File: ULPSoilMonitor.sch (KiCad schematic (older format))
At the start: 21 parts, among them Q3 BC817, Q4 MMDT3904, SW1 RESET, U1 ESP32-WROOM-32, U2 MCP73123

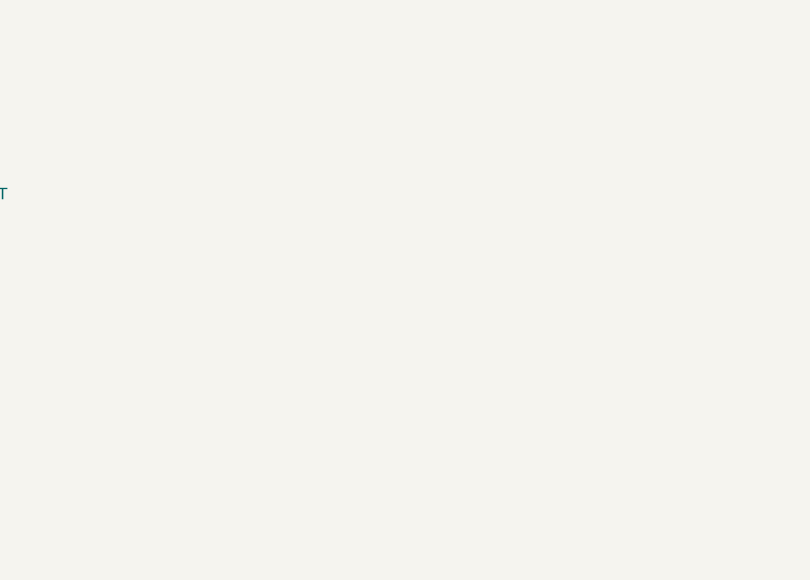
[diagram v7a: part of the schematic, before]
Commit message: Add USB-C connector
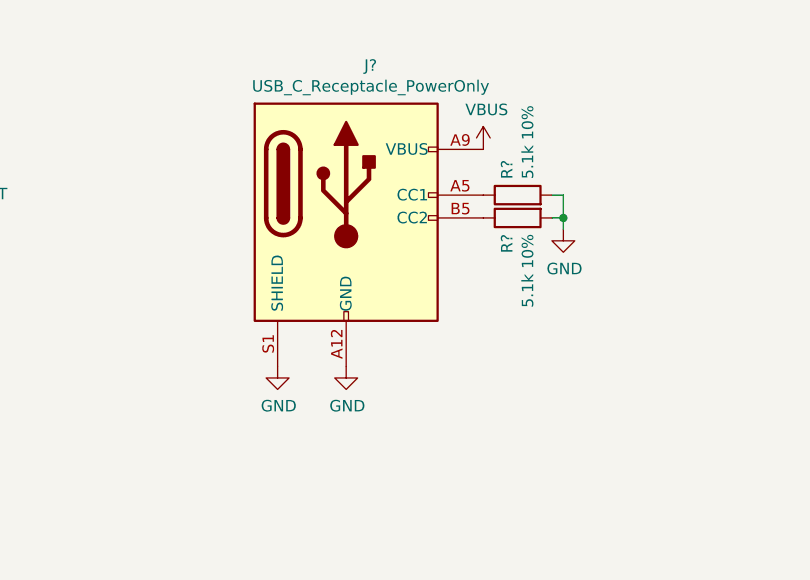
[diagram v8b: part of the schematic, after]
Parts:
- added J?: USB_C_Receptacle_PowerOnly, 0 - GIE Connectors, Terminal Blocks:TYPE-C-31-M-17.kicad_mod, symbol 0-GIE_Connector_Debug:USB_C_Receptacle_PowerOnly
- added R? (x2): 5.1k 10%, Resistor_SMD:R_0805_2012Metric, symbol Device:R
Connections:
- net -BATT: now also J?.A12 (GND), J?.B12 (GND), J?.S1 (SHIELD), R?.2, R?.2
- net VBUS: now also J?.A9 (VBUS), J?.B9 (VBUS)
- new net: J?.A5 (CC1), R?.1
- new net: J?.B5 (CC2), R?.1
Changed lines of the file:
@@
 Wire Wire Line
 	9400 5900 9400 6200
+$Comp
+L 0-GIE_Connector_Debug:USB_C_Receptacle_PowerOnly J?
+U 1 1 60612B67
+P 8500 1300
+F 0 "J?" H 8607 1817 50  0000 C CNN
+F 1 "USB_C_Receptacle_PowerOnly" H 8607 1726 50  0000 C CNN
+F 2 "0 - GIE Connectors, Terminal Blocks:TYPE-C-31-M-17.kicad_mod" H 8650 1800 50  0001 C CNN
+F 3 "https://www.usb.org/sites/default/files/documents/usb_type-c.zip" H 8650 1300 50  0001 C CNN
+	1    8500 1300
+	1    0    0    -1
+$EndComp
+$Comp
+L power:GND #PWR?
+U 1 1 60613D10
+P 8200 2100
+F 0 "#PWR?" H 8200 1850 50  0001 C CNN
+F 1 "GND" H 8205 1927 50  0000 C CNN
+F 2 "" H 8200 2100 50  0001 C CNN
+F 3 "" H 8200 2100 50  0001 C CNN
+	1    8200 2100
+	1    0    0    -1
+$EndComp
+$Comp
+L power:GND #PWR?
+U 1 1 60614146
+P 8500 2100
+F 0 "#PWR?" H 8500 1850 50  0001 C CNN
+F 1 "GND" H 8505 1927 50  0000 C CNN
+F 2 "" H 8500 2100 50  0001 C CNN
+F 3 "" H 8500 2100 50  0001 C CNN
+	1    8500 2100
+	1    0    0    -1
+$EndComp
+$Comp
+L power:VBUS #PWR?
+U 1 1 6061444E
+P 9100 1150
+F 0 "#PWR?" H 9100 1000 50  0001 C CNN
+F 1 "VBUS" H 9115 1323 50  0000 C CNN
+F 2 "" H 9100 1150 50  0001 C CNN
+F 3 "" H 9100 1150 50  0001 C CNN
+	1    9100 1150
+	1    0    0    -1
+$EndComp
+$Comp
+L Device:R R?
+U 1 1 60614C20
+P 9250 1350
+F 0 "R?" H 9320 1396 50  0000 L CNN
+F 1 "5.1k 10%" H 9320 1305 50  0000 L CNN
+F 2 "Resistor_SMD:R_0805_2012Metric" V 9180 1350 50  0001 C CNN
+F 3 "~" H 9250 1350 50  0001 C CNN
+F 4 "C17513" H 9250 1350 50  0001 C CNN "LCSC"
+	1    9250 1350
+	0    -1   -1   0
+$EndComp
+$Comp
+L Device:R R?
+U 1 1 60615957
+P 9250 1450
+F 0 "R?" H 9320 1496 50  0000 L CNN
+F 1 "5.1k 10%" H 9320 1405 50  0000 L CNN
+F 2 "Resistor_SMD:R_0805_2012Metric" V 9180 1450 50  0001 C CNN
+F 3 "~" H 9250 1450 50  0001 C CNN
+F 4 "C17513" H 9250 1450 50  0001 C CNN "LCSC"
+	1    9250 1450
+	0    -1   1    0
+$EndComp
+$Comp
+L power:GND #PWR?
+U 1 1 60619E98
+P 9450 1500
+F 0 "#PWR?" H 9450 1250 50  0001 C CNN
+F 1 "GND" H 9455 1327 50  0000 C CNN
+F 2 "" H 9450 1500 50  0001 C CNN
+F 3 "" H 9450 1500 50  0001 C CNN
+	1    9450 1500
+	1    0    0    -1
+$EndComp
+Wire Wire Line
+	9450 1500 9450 1450
+Wire Wire Line
+	9450 1450 9400 1450
+Wire Wire Line
+	9400 1350 9450 1350
+Wire Wire Line
+	9450 1350 9450 1450
+Connection ~ 9450 1450
 $EndSCHEMATC
